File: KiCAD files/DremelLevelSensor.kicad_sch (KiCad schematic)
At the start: 6 parts

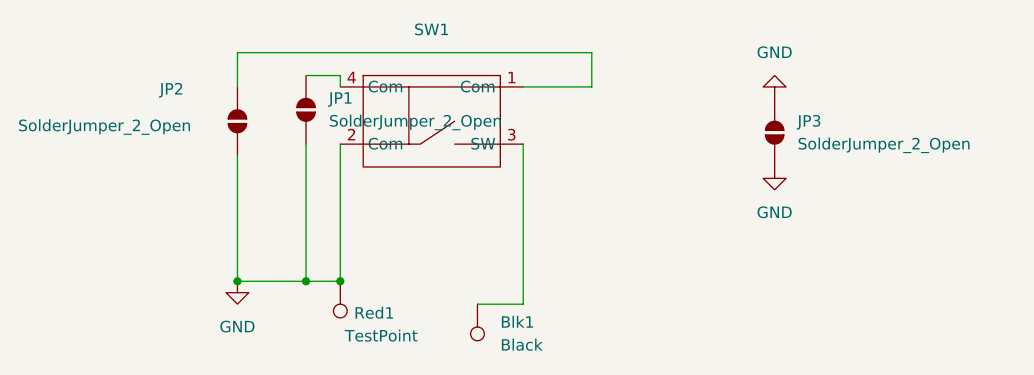
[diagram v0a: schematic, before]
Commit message: Update PCB and Schematic to remove unnecessary jumper that was added to try to get DKRed to work
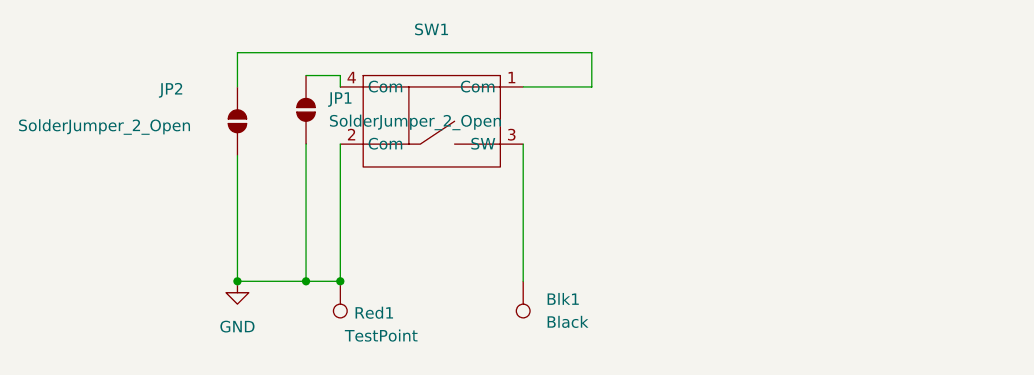
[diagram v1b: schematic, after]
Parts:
- removed JP3: SolderJumper_2_Open, Jumper:SolderJumper-2_P1.3mm_Open_RoundedPad1.0x1.5mm, symbol Jumper:SolderJumper_2_Open
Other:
- moved on the sheet: Blk1
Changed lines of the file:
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@@
-	(wire
-		(pts
-			(xy 113.03 86.36) (xy 113.03 104.14)
-		)
-		(stroke
-			(width 0)
-			(type default)
-		)
-	)
 	(wire
 		(pts
@@
 	(wire
 		(pts
-			(xy 113.03 104.14) (xy 107.95 104.14)
-		)
-		(stroke
-			(width 0)
-			(type default)
-		)
-	)
-	(wire
-		(pts
 			(xy 88.9 86.36) (xy 88.9 101.6)
+		)
+		(stroke
+			(width 0)
+			(type default)
+		)
+	)
+	(wire
+		(pts
+			(xy 113.03 86.36) (xy 113.03 101.6)
 		)
 		(stroke
@@
 	)
 	(symbol
-		(lib_id "power:GND")
-		(at 140.97 81.28 180)
-		(unit 1)
-		(exclude_from_sim no)
-		(in_bom yes)
-		(on_board yes)
-		(dnp no)
-		(fields_autoplaced yes)
-		(property "Reference" "#PWR03"
-			(at 140.97 74.93 0)
-			(effects
-				(font
-					(size 1.27 1.27)
-				)
-				(hide yes)
-			)
-		)
-		(property "Value" "GND"
-			(at 140.97 76.2 0)
-			(effects
-				(font
-					(size 1.27 1.27)
-				)
-			)
-		)
-		(property "Footprint" ""
-			(at 140.97 81.28 0)
-			(effects
-				(font
-					(size 1.27 1.27)
-				)
-				(hide yes)
-			)
-		)
-		(property "Datasheet" ""
-			(at 140.97 81.28 0)
-			(effects
-				(font
-					(size 1.27 1.27)
-				)
-				(hide yes)
-			)
-		)
-		(property "Description" "Power symbol creates a global label with name \"GND\" , ground"
-			(at 140.97 81.28 0)
-			(effects
-				(font
-					(size 1.27 1.27)
-				)
-				(hide yes)
-			)
-		)
-		(pin "1"
-		)
-		(instances
-			(project "DremelLevelSensor"
-				(path "/7accf362-abd1-4df7-ad78-69f9d0334dcd"
-					(reference "#PWR03")
-					(unit 1)
-				)
-			)
-		)
-	)
-	(symbol
-		(lib_id "power:GND")
-		(at 140.97 88.9 0)
-		(unit 1)
-		(exclude_from_sim no)
-		(in_bom yes)
-		(on_board yes)
-		(dnp no)
-		(fields_autoplaced yes)
-		(property "Reference" "#PWR02"
-			(at 140.97 95.25 0)
-			(effects
-				(font
-					(size 1.27 1.27)
-				)
-				(hide yes)
-			)
-		)
-		(property "Value" "GND"
-			(at 140.97 93.98 0)
-			(effects
-				(font
-					(size 1.27 1.27)
-				)
-			)
-		)
-		(property "Footprint" ""
-			(at 140.97 88.9 0)
-			(effects
-				(font
-					(size 1.27 1.27)
-				)
-				(hide yes)
-			)
-		)
-		(property "Datasheet" ""
-			(at 140.97 88.9 0)
-			(effects
-				(font
-					(size 1.27 1.27)
-				)
-				(hide yes)
-			)
-		)
-		(property "Description" "Power symbol creates a global label with name \"GND\" , ground"
-			(at 140.97 88.9 0)
-			(effects
-				(font
-					(size 1.27 1.27)
-				)
-				(hide yes)
-			)
-		)
-		(pin "1"
-		)
-		(instances
-			(project "DremelLevelSensor"
-				(path "/7accf362-abd1-4df7-ad78-69f9d0334dcd"
-					(reference "#PWR02")
-					(unit 1)
-				)
-			)
-		)
-	)
-	(symbol
 		(lib_id "Connector:TestPoint")
-		(at 107.95 104.14 180)
+		(at 113.03 101.6 180)
 		(unit 1)
 		(exclude_from_sim no)
@@
 		(fields_autoplaced yes)
 		(property "Reference" "Blk1"
-			(at 110.49 106.1719 0)
+			(at 115.57 103.6319 0)
 			(effects
 				(font
@@
 		)
 		(property "Value" "Black"
-			(at 110.49 108.7119 0)
+			(at 115.57 106.1719 0)
 			(effects
 				(font
@@
 		)
 		(property "Footprint" "TestPoint:TestPoint_Pad_D1.5mm"
-			(at 102.87 104.14 0)
+			(at 107.95 101.6 0)
 			(effects
 				(font
@@
 		)
 		(property "Datasheet" "~"
-			(at 102.87 104.14 0)
+			(at 107.95 101.6 0)
 			(effects
 				(font
@@
 		)
 		(property "Description" "test point"
-			(at 107.95 104.14 0)
+			(at 113.03 101.6 0)
 			(effects
 				(font
@@
 					(unit 1)
 				)
-			)
-		)
-	)
-	(symbol
-		(lib_id "Jumper:SolderJumper_2_Open")
-		(at 140.97 85.09 90)
-		(unit 1)
-		(exclude_from_sim no)
-		(in_bom no)
-		(on_board yes)
-		(dnp no)
-		(fields_autoplaced yes)
-		(property "Reference" "JP3"
-			(at 143.51 83.8199 90)
-			(effects
-				(font
-					(size 1.27 1.27)
-				)
-				(justify right)
-			)
-		)
-		(property "Value" "SolderJumper_2_Open"
-			(at 143.51 86.3599 90)
-			(effects
-				(font
-					(size 1.27 1.27)
-				)
-				(justify right)
-			)
-		)
-		(property "Footprint" "Jumper:SolderJumper-2_P1.3mm_Open_RoundedPad1.0x1.5mm"
-			(at 140.97 85.09 0)
-			(effects
-				(font
-					(size 1.27 1.27)
-				)
-				(hide yes)
-			)
-		)
-		(property "Datasheet" "~"
-			(at 140.97 85.09 0)
-			(effects
-				(font
-					(size 1.27 1.27)
-				)
-				(hide yes)
-			)
-		)
-		(property "Description" "Solder Jumper, 2-pole, open"
-			(at 140.97 85.09 0)
-			(effects
-				(font
-					(size 1.27 1.27)
-				)
-				(hide yes)
-			)
-		)
-		(pin "2"
-		)
-		(pin "1"
-		)
-		(instances
-			(project "DremelLevelSensor"
-				(path "/7accf362-abd1-4df7-ad78-69f9d0334dcd"
-					(reference "JP3")
-					(unit 1)
-				)
